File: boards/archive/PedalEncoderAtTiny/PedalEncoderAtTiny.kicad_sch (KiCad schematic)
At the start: 33 parts, among them J1 Pwr, J2 Control, J3 Switch, J4 ISP, J5 Pedal, J6 MIDI Out, J7 I2C, Q1 BC547, U1 4069, U2 ATmega48-20P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

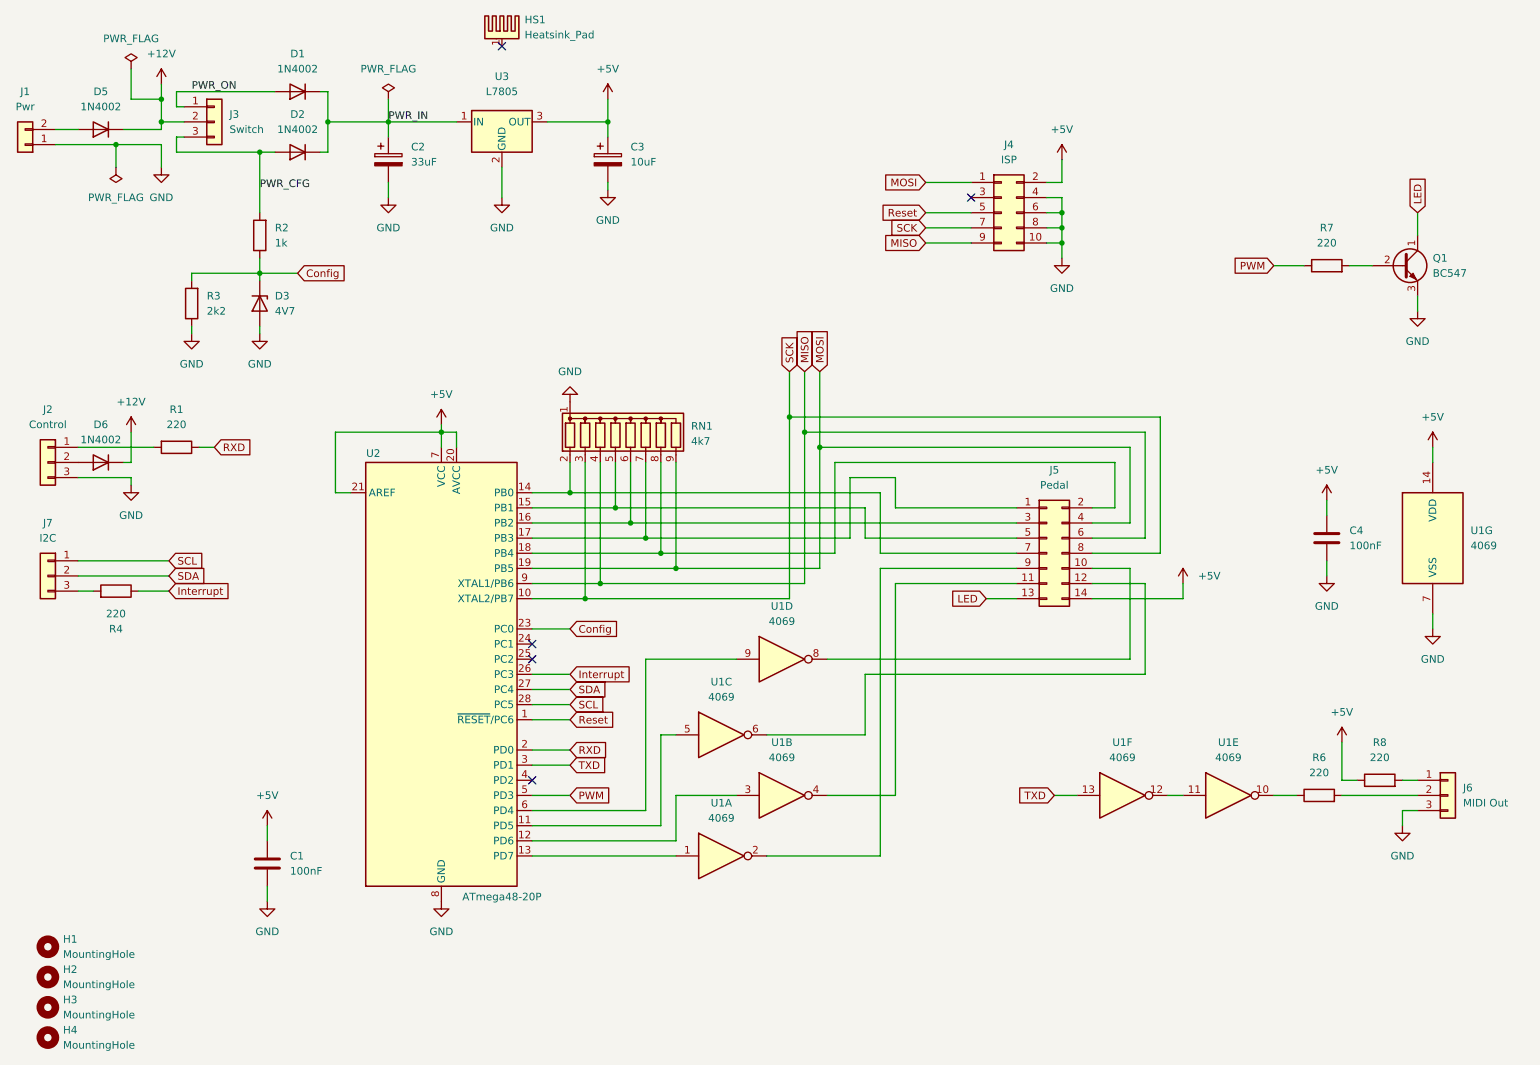
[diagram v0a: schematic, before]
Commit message: Updated to KiCAD 8, fixed optocouplers for MIDI and added powersupplies
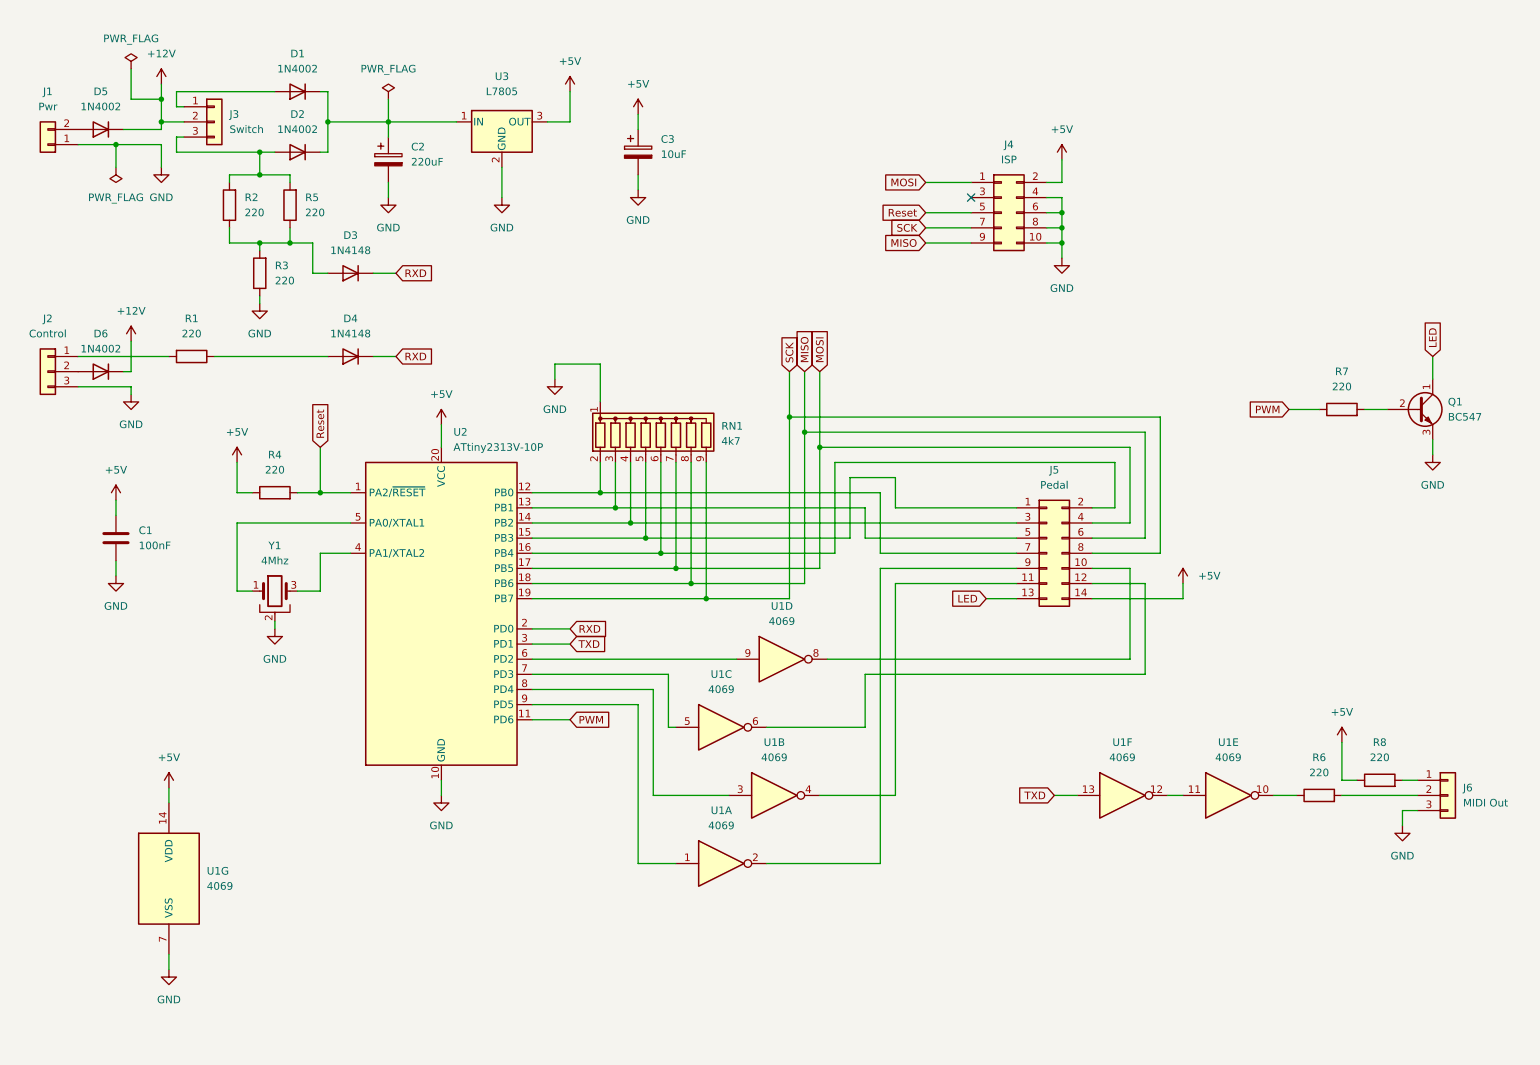
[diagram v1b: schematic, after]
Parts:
- removed C4: 100nF, Capacitor_THT:C_Disc_D7.5mm_W2.5mm_P5.00mm, symbol Device:C
- removed D3: 4V7, Diode_THT:D_DO-15_P2.54mm_Vertical_AnodeUp, symbol Device:D_Zener
- removed H1, H2, H3, H4: MountingHole, MountingHole:MountingHole_3mm, symbol Mechanical:MountingHole
- removed HS1: Heatsink_Pad, Heatsink:Heatsink_AAVID_576802B03900G, symbol Mechanical:Heatsink_Pad
- removed J7: I2C, Connector_PinHeader_2.54mm:PinHeader_1x03_P2.54mm_Vertical, symbol Connector_Generic:Conn_01x03
- removed U2: ATmega48-20P, Package_DIP:DIP-28_W7.62mm_Socket, symbol MCU_Microchip_ATmega:ATmega48-20P
- added D3, D4: 1N4148, Diode_THT:D_DO-35_SOD27_P7.62mm_Horizontal, symbol Diode:1N4148
- added R5: 220, Resistor_THT:R_Axial_DIN0204_L3.6mm_D1.6mm_P2.54mm_Vertical, symbol Device:R
- added U2: ATtiny2313V-10P, Package_DIP:DIP-20_W7.62mm, symbol MCU_Microchip_ATtiny:ATtiny2313V-10P
- added Y1: 4Mhz, Crystal:Crystal_HC49-U-3Pin_Vertical, symbol Device:Crystal_GND2
- C2: value 33uF -> 220uF; footprint Capacitor_THT:CP_Radial_D8.0mm_P2.50mm -> Capacitor_THT:CP_Radial_D10.0mm_P5.00mm
- D1, D2: footprint Diode_THT:D_DO-41_SOD81_P2.54mm_Vertical_AnodeUp -> Diode_THT:D_DO-41_SOD81_P10.16mm_Horizontal
- D5, D6: footprint Diode_THT:D_DO-41_SOD81_P7.62mm_Horizontal -> Diode_THT:D_DO-41_SOD81_P10.16mm_Horizontal
- R1, R7: footprint Resistor_THT:R_Axial_DIN0204_L3.6mm_D1.6mm_P7.62mm_Horizontal -> Resistor_THT:R_Axial_DIN0204_L3.6mm_D1.6mm_P2.54mm_Vertical
- R2: value 1k -> 220; footprint Resistor_THT:R_Axial_DIN0204_L3.6mm_D1.6mm_P7.62mm_Horizontal -> Resistor_THT:R_Axial_DIN0204_L3.6mm_D1.6mm_P2.54mm_Vertical
- R3: value 2k2 -> 220
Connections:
- net Interrupt is gone; now on net +5V: R4.1
- net +5V: now also U2.20 (VCC)
- net GND: now also U2.10 (GND), Y1.2
- net MISO: now also RN1.8 (R7), U2.18 (PB6); no longer RN1.4 (R3)
- net MOSI: now also RN1.7 (R6), U2.17 (PB5); no longer RN1.9 (R8)
- net PWM: now also U2.11 (PD6)
- net RXD: now also D3.1 (K), D4.1 (K), U2.2 (PD0); no longer R1.1
- net Reset: now also R4.2, U2.1 (PA2/~{RESET})
- net SCK: now also RN1.9 (R8), U2.19 (PB7); no longer RN1.3 (R2)
- net TXD: now also U2.3 (PD1)
- net at J5.7 (Pin_7), RN1.2 (R1): now also U2.12 (PB0)
- net at J5.5 (Pin_5): now also RN1.3 (R2), U2.13 (PB1); no longer RN1.5 (R4)
- net at J5.3 (Pin_3): now also RN1.4 (R3), U2.14 (PB2); no longer RN1.6 (R5)
- net at J5.1 (Pin_1): now also RN1.5 (R4), U2.15 (PB3); no longer RN1.7 (R6)
- net at J5.2 (Pin_2): now also RN1.6 (R5), U2.16 (PB4); no longer RN1.8 (R7)
- net at U1.9: now also U2.6 (PD2)
- net at U1.5: now also U2.7 (PD3)
- net at U1.3: now also U2.8 (PD4)
- net at U1.1: now also U2.9 (PD5)
- net Config: no longer names the net of R2.1, R3.2
- net Config: now also D3.2 (A), R5.1
- net PWR_CFG: no longer names the net of D2.2 (A), J3.3 (Pin_3), R2.2
- net PWR_CFG: now also R5.2
- net PWR_IN: no longer names the net of C2.1, D1.1 (K), D2.1 (K), U3.1 (IN)
- net PWR_ON: no longer names the net of D1.2 (A), J3.1 (Pin_1)
- new net: D4.2 (A), R1.1
- new net: U2.5 (PA0/XTAL1), Y1.1
- new net: U2.4 (PA1/XTAL2), Y1.3
- no-connect marks 5 -> 1
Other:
- moved on the sheet: C1, C3, D6, J1, J2, Q1, R1, R2, R7, RN1, U1A, U1B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
